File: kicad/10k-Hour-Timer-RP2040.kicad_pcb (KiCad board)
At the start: 2 copper layers, 245 x 173 mm, 105 parts, among them J1 JST_SH_SM03B, J2 USB_C_Receptacle_USB2.0_16P, J3 S2B-PH-K-S_LF__SN_, Q1 PMOS, Q2 AO3400A, Q3 AO3400A, Q4 AO3400A, Q5 AO3400A, U1 USBLC6-2SC6, U2 MCP73831-2-OT, U3 BQ29700DSER, U4 TLV62568DBVR, U5 W25Q128JVS, U6 PCF8523T, U7 RP2040, Y1 ABS07AIG-32.768KHZ-7-T, Y2 ABM8-272-T3

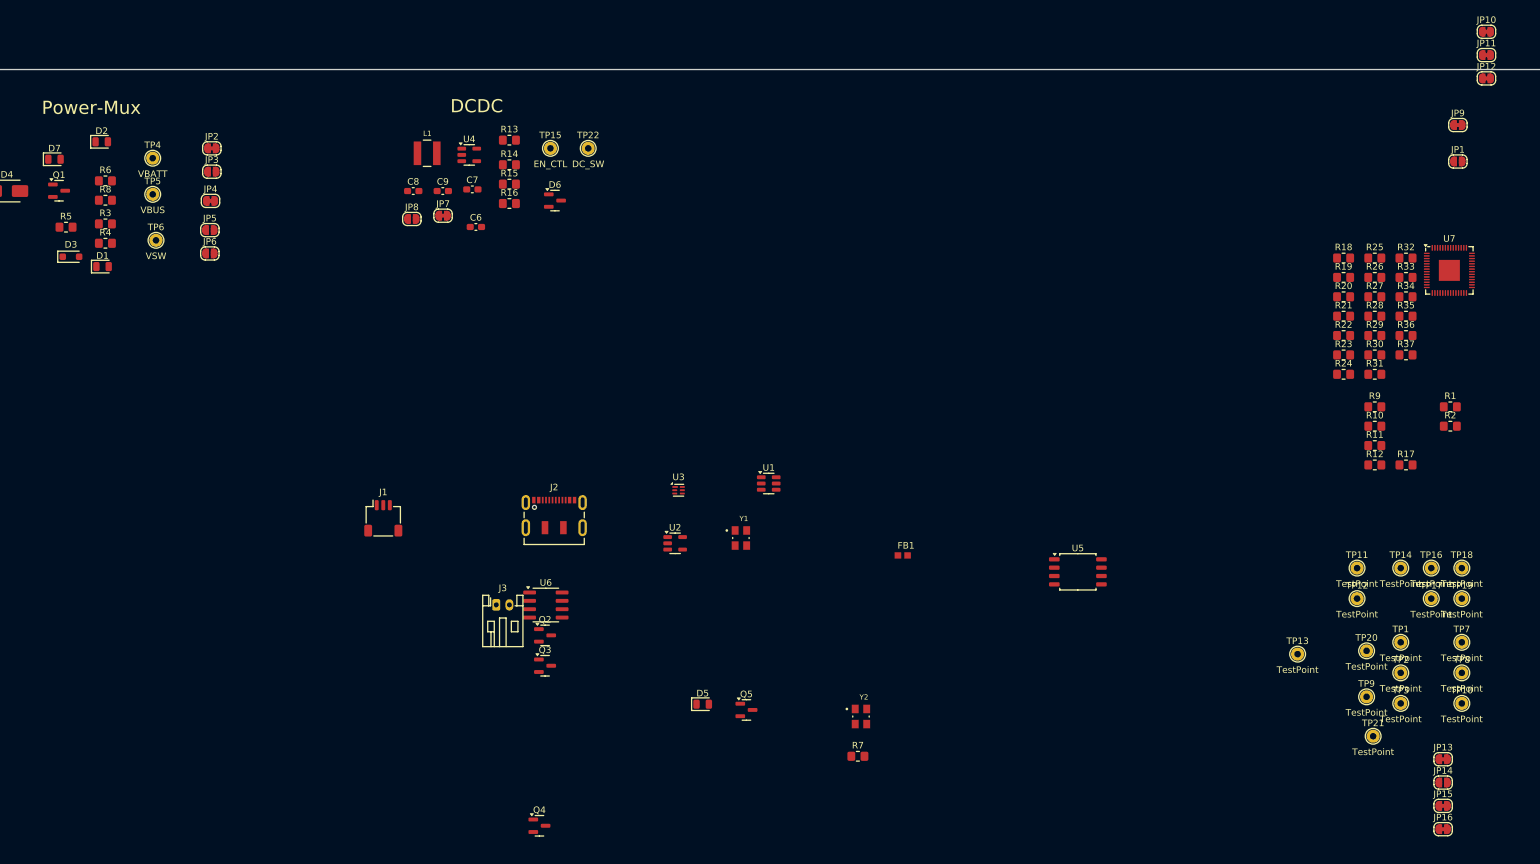
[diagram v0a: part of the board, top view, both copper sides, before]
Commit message: led indicator silks
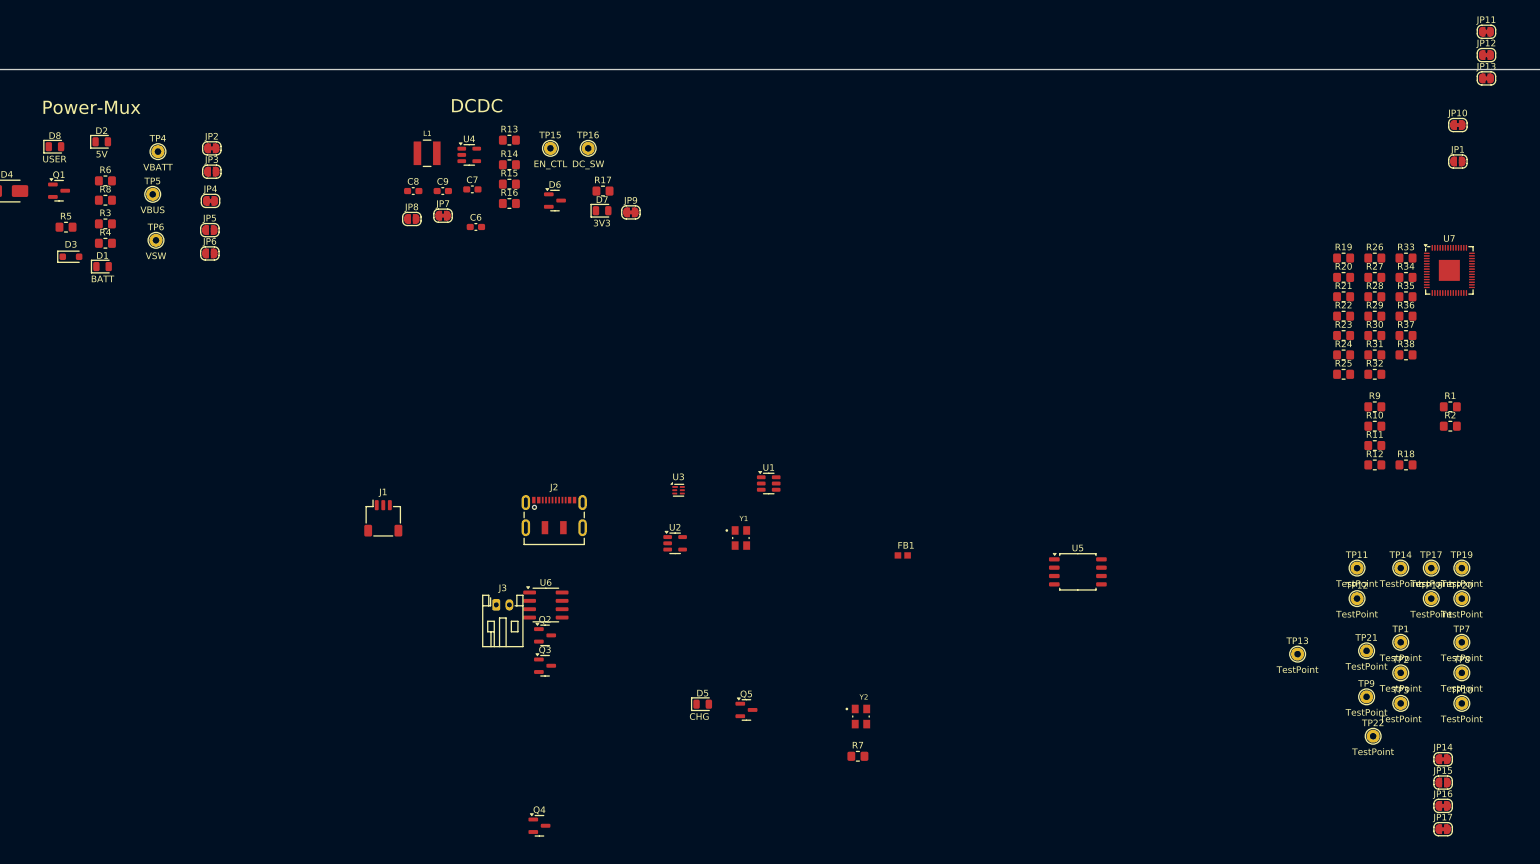
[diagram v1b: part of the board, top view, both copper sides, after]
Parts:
- added D7: 3V3, LED_SMD:LED_0805_2012Metric, F.Cu at (128.6, 38.5)
- added JP9: SolderJumper_2_Bridged, Jumper:SolderJumper-2_P1.3mm_Bridged_RoundedPad1.0x1.5mm, F.Cu at (133.0, 38.8)
- added R17: 1K, Resistor_SMD:R_0805_2012Metric_Pad1.20x1.40mm_HandSolder, F.Cu at (128.8, 35.5)
- D8: renamed from D7; value RED -> USER
- moved D8 1.91 mm to (45.3, 28.8)
- moved TP4 1.28 mm to (61.0, 29.5)
- renumbered JP9 to JP10, JP10 to JP11, JP11 to JP12, JP12 to JP13, JP13 to JP14, JP14 to JP15, JP15 to JP16, JP16 to JP17, R17 to R18, R18 to R19, R19 to R20, R20 to R21, R21 to R22, R22 to R23, R23 to R24, R24 to R25, R25 to R26, R26 to R27, R27 to R28, R28 to R29, R29 to R30, R30 to R31, R31 to R32, R32 to R33, R33 to R34, R34 to R35, R35 to R36, R36 to R37, R37 to R38, TP22 to TP16, TP16 to TP17, TP17 to TP18, TP18 to TP19, TP19 to TP20, TP20 to TP21, TP21 to TP22

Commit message: DR SYS-03 Charger ✅
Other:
- board text added: "RP2040 WOD Timer Eval Board"
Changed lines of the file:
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@@
+		)
+	)
+	(gr_text "RP2040 WOD Timer Eval Board"
+		(at 37 152.25 0)
+		(layer "F.SilkS")
+		(effects
+			(font
+				(size 1 1)
+				(thickness 0.1)
+			)
+			(justify left bottom)
 		)
 	)

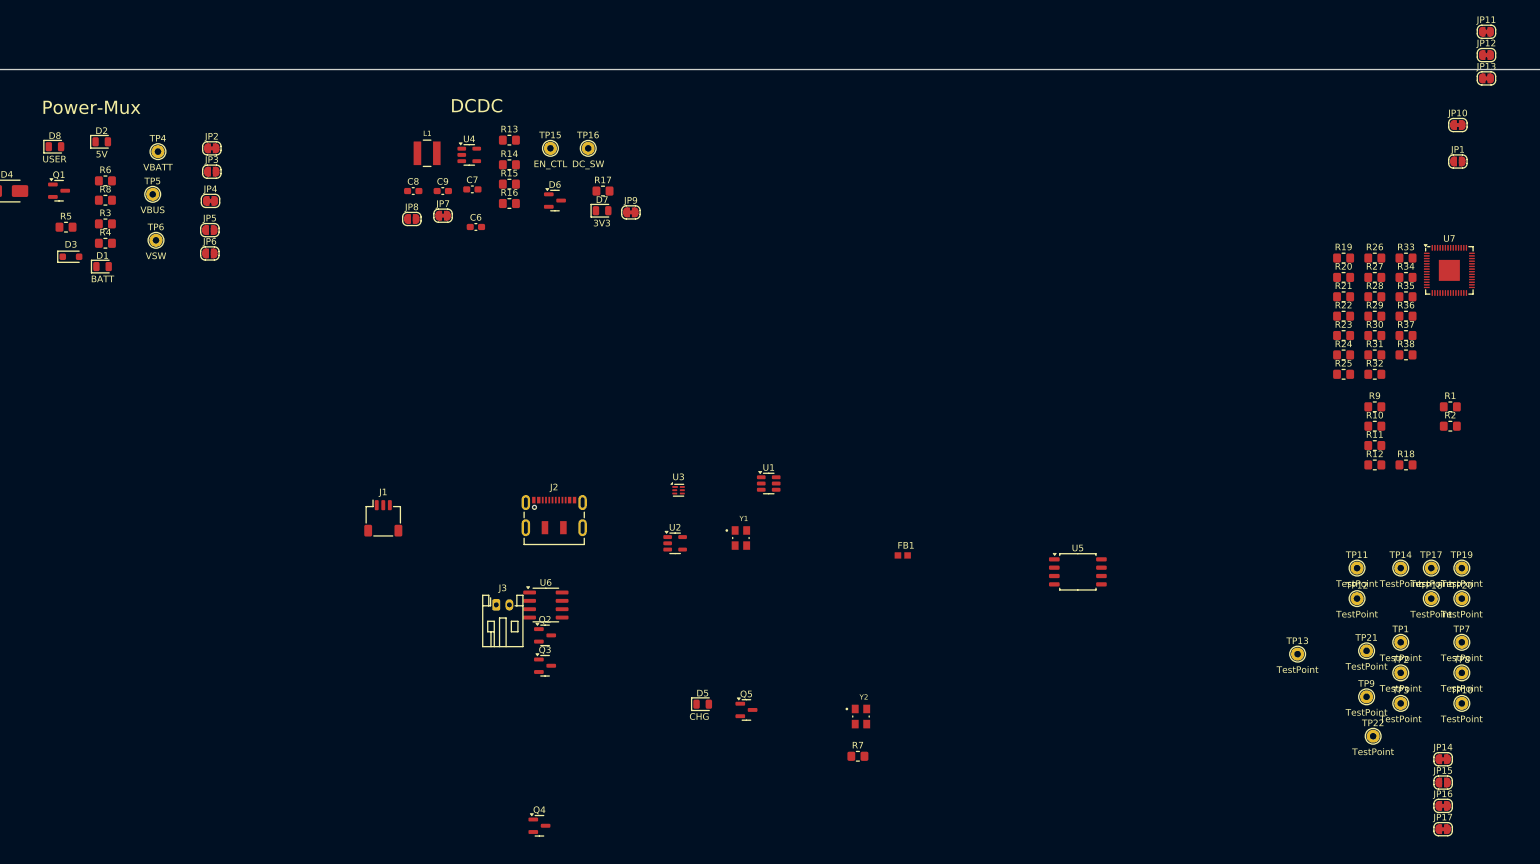
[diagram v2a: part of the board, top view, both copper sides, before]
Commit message: charger pcb update
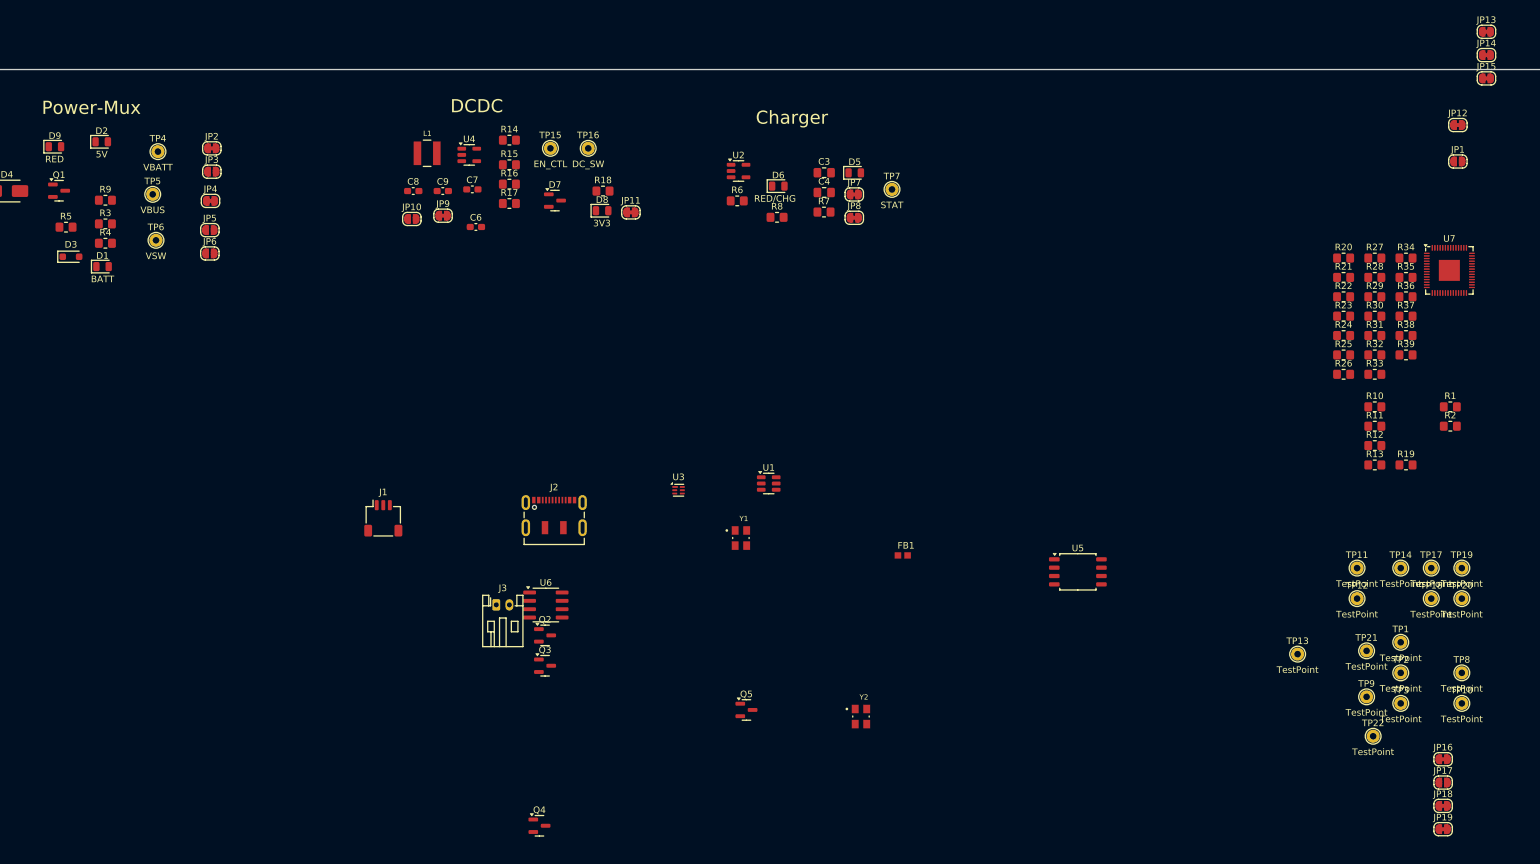
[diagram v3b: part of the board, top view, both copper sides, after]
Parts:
- added C3: 4.7u, Capacitor_SMD:C_0805_2012Metric_Pad1.18x1.45mm_HandSolder, F.Cu at (162.4, 32.7)
- added C4: 4.7u, Capacitor_SMD:C_0805_2012Metric_Pad1.18x1.45mm_HandSolder, F.Cu at (162.4, 35.7)
- added D5: GRN/DONE, LED_SMD:LED_0805_2012Metric, F.Cu at (167.1, 32.7)
- added JP7: SolderJumper_2_Bridged, Jumper:SolderJumper-2_P1.3mm_Bridged_RoundedPad1.0x1.5mm, F.Cu at (167.0, 36.0)
- added JP8: SolderJumper_2_Bridged, Jumper:SolderJumper-2_P1.3mm_Bridged_RoundedPad1.0x1.5mm, F.Cu at (167.0, 39.6)
- added R7: 2K, Resistor_SMD:R_0805_2012Metric_Pad1.20x1.40mm_HandSolder, F.Cu at (162.4, 38.7)
- D6: renamed from D5; value CHG -> RED/CHG
- D9: renamed from D8; value USER -> RED
- R18: renamed from R17; value 1K -> 2K
- R6: value 2K -> 3K
- TP7: value TestPoint -> STAT
- moved TP7 110.8 mm to (172.8, 35.2)
- moved R6 96.2 mm to (149.2, 37.0)
- moved R8 83.0 mm to (155.2, 39.5)
- moved D6 79.7 mm to (155.4, 34.8)
- moved U2 57.5 mm to (149.4, 32.5)
- renumbered D6 to D7, D7 to D8, JP8 to JP10, JP9 to JP11, JP10 to JP12, JP11 to JP13, JP12 to JP14, JP13 to JP15, JP14 to JP16, JP15 to JP17, JP16 to JP18, JP17 to JP19, JP7 to JP9, R9 to R10, R10 to R11, R11 to R12, R12 to R13, R13 to R14, R14 to R15, R15 to R16, R16 to R17, R18 to R19, R19 to R20, R20 to R21, R21 to R22, R22 to R23, R23 to R24, R24 to R25, R25 to R26, R26 to R27, R27 to R28, R28 to R29, R29 to R30, R30 to R31, R31 to R32, R32 to R33, R33 to R34, R34 to R35, R35 to R36, R36 to R37, R37 to R38, R38 to R39, R7 to R8, R8 to R9
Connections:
- D6 pad 2: /01-04-Power-DCDC-Charger-Battery/5V_USB -> Net-(D6-A)
- R8 pad 1: Net-(U2-STAT) -> /01-04-Power-DCDC-Charger-Battery/STAT
- TP7 pad 1: /01-04-Power-DCDC-Charger-Battery/5V_USB -> /01-04-Power-DCDC-Charger-Battery/STAT
- U2 pad 1: Net-(U2-STAT) -> /01-04-Power-DCDC-Charger-Battery/STAT
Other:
- board text added: "Charger"

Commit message: DR SYS-04-Battery Protect ✅
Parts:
- added C5: 0.1u, Capacitor_SMD:C_0805_2012Metric_Pad1.18x1.45mm_HandSolder, F.Cu at (206.7, 42.7)
- added JP10: SolderJumper_2_Open, Jumper:SolderJumper-2_P1.3mm_Open_RoundedPad1.0x1.5mm, F.Cu at (202.2, 46.5)
- added JP9: SolderJumper_2_Bridged, Jumper:SolderJumper-2_P1.3mm_Bridged_RoundedPad1.0x1.5mm, F.Cu at (202.2, 43.0)
- added TP9: BAT-, project footprints:TestPoint_THTPad_D2.0mm_Drill1.0mm, F.Cu at (206.3, 46.2)
- TP10: renamed from TP9; value TestPoint -> U3_V-
- TP11: renamed from TP10; value TestPoint -> DSG
- TP12: renamed from TP11; value TestPoint -> CHG
- TP13: renamed from TP12; value TestPoint -> GND
- TP14: renamed from TP13; value TestPoint -> Q23_D
- TP15: renamed from TP14; value TestPoint -> BAT-
- TP8: value TestPoint -> BAT+
- moved R9 151.3 mm to (204.2, 37.0)
- moved Q2 104.0 mm to (196.4, 32.6)
- moved Q3 103.4 mm to (196.4, 38.1)
- moved J3 96.5 mm to (187.2, 37.5)
- moved TP8 80.4 mm to (213.0, 43.2)
- moved TP10 80.2 mm to (218.8, 36.7)
- moved TP11 78.7 mm to (213.0, 50.0)
- moved TP15 70.1 mm to (218.8, 30.2)
- moved TP12 70.1 mm to (212.8, 29.9)
- moved TP13 68.2 mm to (212.8, 36.7)
- moved U3 67.1 mm to (195.5, 43.0)
- moved TP14 64.1 mm to (218.5, 44.0)
- moved R13 41.4 mm to (225.2, 41.5)
- moved R10 41.4 mm to (225.2, 32.7)
- moved R11 41.4 mm to (225.2, 35.6)
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- renumbered JP9 to JP11, JP10 to JP12, JP11 to JP13, JP12 to JP14, JP13 to JP15, JP14 to JP16, JP15 to JP17, JP16 to JP18, JP17 to JP19, JP18 to JP20, JP19 to JP21, TP15 to TP16, TP16 to TP17, TP17 to TP18, TP18 to TP19, TP19 to TP20, TP20 to TP21, TP21 to TP22, TP22 to TP23
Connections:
- R10 pad 1: Net-(U3-BAT) -> Net-(JP10-B)
- U3 pad 5: Net-(U3-BAT) -> Net-(JP10-A)
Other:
- board text added: "Batt Protect"

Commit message: DR SYS-05-MCU XTAL
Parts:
- added C10: 15p, Capacitor_SMD:C_0603_1608Metric_Pad1.08x0.95mm_HandSolder, F.Cu at (111.6, 73.5)
- added C11: 15p, Capacitor_SMD:C_0603_1608Metric_Pad1.08x0.95mm_HandSolder, F.Cu at (111.6, 76.0)
- added C13: 2.2u, Capacitor_SMD:C_0805_2012Metric_Pad1.18x1.45mm_HandSolder, F.Cu at (48.0, 75.8)
- added C14: 100n, Capacitor_SMD:C_0805_2012Metric_Pad1.18x1.45mm_HandSolder, F.Cu at (48.0, 78.8)
- added C17: 1u, Capacitor_SMD:C_0805_2012Metric_Pad1.18x1.45mm_HandSolder, F.Cu at (82.0, 69.0)
- added C18: 100n, Capacitor_SMD:C_0805_2012Metric_Pad1.18x1.45mm_HandSolder, F.Cu at (82.0, 72.0)
- added C19: 100n, Capacitor_SMD:C_0805_2012Metric_Pad1.18x1.45mm_HandSolder, F.Cu at (82.0, 75.0)
- added C20: 1u, Capacitor_SMD:C_0805_2012Metric_Pad1.18x1.45mm_HandSolder, F.Cu at (82.0, 78.0)
- added C21: 100n, Capacitor_SMD:C_0805_2012Metric_Pad1.18x1.45mm_HandSolder, F.Cu at (82.0, 81.0)
- added C22: 100n, Capacitor_SMD:C_0805_2012Metric_Pad1.18x1.45mm_HandSolder, F.Cu at (82.0, 84.0)
- added C23: 1u, Capacitor_SMD:C_0805_2012Metric_Pad1.18x1.45mm_HandSolder, F.Cu at (82.0, 87.1)
- added J8: Conn_01x03_Pin, Connector_PinHeader_2.54mm:PinHeader_1x03_P2.54mm_Vertical, F.Cu at (121.0, 76.0)
- added SW1: BOOTSEL, Button_Switch_THT:SW_PUSH_6mm, F.Cu at (30.0, 75.0)
- added SW2: RESET, Button_Switch_THT:SW_PUSH_6mm, F.Cu at (99.8, 81.0)
- added SW3: USER_A, Button_Switch_THT:SW_PUSH_6mm, F.Cu at (-13.0, 27.7)
- added SW4: USER_B_PWR, Button_Switch_THT:SW_PUSH_6mm, F.Cu at (-13.0, 36.2)
- C7: value 470n -> 470n, 10V
- moved R20 201.4 mm to (42.0, 73.8)
- moved R22 201.2 mm to (42.0, 78.0)
- moved U7 168.9 mm to (91.6, 78.7)
- moved R32 157.8 mm to (90.8, 87.2)
- moved U5 144.7 mm to (57.2, 77.2)
- moved R24 140.2 mm to (102.5, 75.8)
- moved R27 139.8 mm to (111.8, 83.8)
- moved Y2 73.1 mm to (107.1, 75.2)
- moved J1 33.7 mm to (128.3, 78.7)
- moved U6 26.1 mm to (128.5, 123.2)
- moved J2 26.1 mm to (129.2, 106.4)
- moved FB1 23.9 mm to (177.3, 114.7)
- moved Q5 23.9 mm to (153.5, 138.2)
- moved U1 23.9 mm to (156.9, 103.7)
- moved Y1 23.9 mm to (152.7, 112.0)
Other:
- board text added: "MCU decoupling"
- board text added: "Memory"

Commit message: DR SYS-06-MCU-IO ✅
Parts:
- added BZ1: PKMCS0909E4000, project footprints:SPKR_PKMCS0909E4000-R1, F.Cu at (-55.6, 128.9)
- added BZ2: Buzzer D=9mm P=5mm, project footprints:Buz-TH_D9.6_P5, F.Cu at (-67.7, 129.2)
- added C24: 100n, Capacitor_SMD:C_0805_2012Metric_Pad1.18x1.45mm_HandSolder, F.Cu at (-45.2, 116.0)
- added C25: 100n, Capacitor_SMD:C_0805_2012Metric_Pad1.18x1.45mm_HandSolder, F.Cu at (-5.08, 121.9)
- added J6: Conn_01x03_Pin, Connector_PinHeader_2.54mm:PinHeader_1x03_P2.54mm_Vertical, F.Cu at (-88.9, 105.2)
- added J7: Conn_01x03_Pin, Connector_PinHeader_2.54mm:PinHeader_1x03_P2.54mm_Vertical, F.Cu at (-54.5, 106.4)
- added J9: Conn_01x12_Pin, Connector_PinHeader_2.54mm:PinHeader_1x12_P2.54mm_Vertical, F.Cu at (-81.5, 99.2)
- added JP22: SolderJumper_2_Open, Jumper:SolderJumper-2_P1.3mm_Open_RoundedPad1.0x1.5mm, F.Cu at (300.6, 54.5)
- added R40: 10K, Resistor_SMD:R_0805_2012Metric_Pad1.20x1.40mm_HandSolder, F.Cu at (300.8, 51.2)
- D9: value RED -> RED/USER
- TP18: value TestPoint -> IOGate
- TP20: value TestPoint -> ADC1
- TP21: value TestPoint -> BTN_B
- TP22: value TestPoint -> BTN_B_IN
- moved JP1 334.8 mm to (-48.9, 162.6)
- moved R1 323.2 mm to (-49.8, 167.6)
- moved R2 323.2 mm to (-49.8, 170.6)
- moved R35 300.5 mm to (-44.8, 102.0)
- moved R36 300.5 mm to (-44.8, 104.9)
- moved R37 300.5 mm to (-44.8, 107.9)
- moved JP20 297.1 mm to (-39.5, 106.0)
- moved JP21 297.1 mm to (-39.5, 109.5)
- moved R31 296.3 mm to (-45.0, 111.7)
- moved TP1 296.2 mm to (-41.0, 158.3)
- moved TP2 296.2 mm to (-41.0, 163.0)
- moved TP3 296.2 mm to (-41.0, 167.6)
- moved TP21 290.0 mm to (-30.0, 114.2)
- moved TP19 285.0 mm to (-30.0, 106.9)
- moved TP18 284.9 mm to (-30.0, 99.5)
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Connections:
- net /05-07_MCU-LED-Driver-Displays/Buzz_N renamed /05-07_MCU-LED-Driver-Displays/BZ2_N
- net /05-07_MCU-LED-Driver-Displays/Buzz_P renamed /05-07_MCU-LED-Driver-Displays/BZ2_P
- net /05-07_MCU-LED-Driver-Displays/GPIO_25_LED renamed /05-07_MCU-LED-Driver-Displays/IO25_LED
- net Net-(U7-ADC_AVDD) renamed /05-07_MCU-LED-Driver-Displays/AVDD
- U7 pad 12: unconnected-(U7-GPIO9-Pad12) -> /05-07_MCU-LED-Driver-Displays/IO9
- U7 pad 13: unconnected-(U7-GPIO10-Pad13) -> /05-07_MCU-LED-Driver-Displays/IO10
- U7 pad 17: unconnected-(U7-GPIO14-Pad17) -> /05-07_MCU-LED-Driver-Displays/IO14
- U7 pad 28: unconnected-(U7-GPIO17-Pad28) -> /05-07_MCU-LED-Driver-Displays/IO17
- U7 pad 29: unconnected-(U7-GPIO18-Pad29) -> /05-07_MCU-LED-Driver-Displays/IO18
- U7 pad 32: unconnected-(U7-GPIO21-Pad32) -> /05-07_MCU-LED-Driver-Displays/IO21
- U7 pad 34: unconnected-(U7-GPIO22-Pad34) -> /05-07_MCU-LED-Driver-Displays/IO22
- U7 pad 4: unconnected-(U7-GPIO2-Pad4) -> /05-07_MCU-LED-Driver-Displays/IO2
- U7 pad 5: unconnected-(U7-GPIO3-Pad5) -> /05-07_MCU-LED-Driver-Displays/IO3
- U7 pad 6: unconnected-(U7-GPIO4-Pad6) -> /05-07_MCU-LED-Driver-Displays/IO4
- U7 pad 7: unconnected-(U7-GPIO5-Pad7) -> /05-07_MCU-LED-Driver-Displays/IO5
- U7 pad 8: unconnected-(U7-GPIO6-Pad8) -> /05-07_MCU-LED-Driver-Displays/BZ1
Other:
- board text added: "Analog In"
- board text added: "MCU IO"
- board text added: "USB"
